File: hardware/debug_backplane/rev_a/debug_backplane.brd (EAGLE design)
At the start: 177.8 x 177.8 mm, 295 parts, among them IC3 FT232RQ, J0 BACKPLANE_GENERIC_MODULE_DEBUG, J1 BACKPLANE_GENERIC_MODULE_DEBUG, J2 PJ-102AH, J3 BACKPLANE_CONTROLLER_MODULE, J4 MICRO_USB_B_HIROSE_ZX62-B-5PA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, J5 MICRO_USB_B_HIROSE_ZX62-B-5PA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, J6 MICRO_USB_B_HIROSE_ZX62-B-5PA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, J8 MICRO_USB_B_HIROSE_ZX62-B-5PA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, J9 MICRO_USB_B_HIROSE_ZX62-B-5PA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, Q1 MOSFET-NCHANNELSMD, Q2 MOSFET-NCHANNELSMD, Q3 MOSFET-NCHANNELSMD, Q4 MOSFET-NCHANNELSMD, Q5 MOSFET-NCHANNELSMD, Q6 MOSFET-NCHANNELSMD, Q7 MOSFET-NCHANNELSMD, Q8 MOSFET-NCHANNELSMD, U1 TUSB2077A, U10 SAM4LC8AA, U11 LTC2941, U12 LTC2941, U13 FT232RQ, U14 SN74LVC2T45, U15 SN74LVC2T45, U16 FT232RQ, U2 FXMA2102, U20 TS3USB30E, U21 TS3USB30E, U26 MCP23008QFN, U27 MCP23008QFN, U3 FXMA2102, U4 MAX8887EZK33+T, U40 FT232RQ, U41 FT232RQ, U5 LTC2941, U6 PCA9544AQFN-N20, U7 LTC2941, U8 SN74LVC2T45, U9 SN74LVC2T45, X1 16MHz, Y1 ABMM

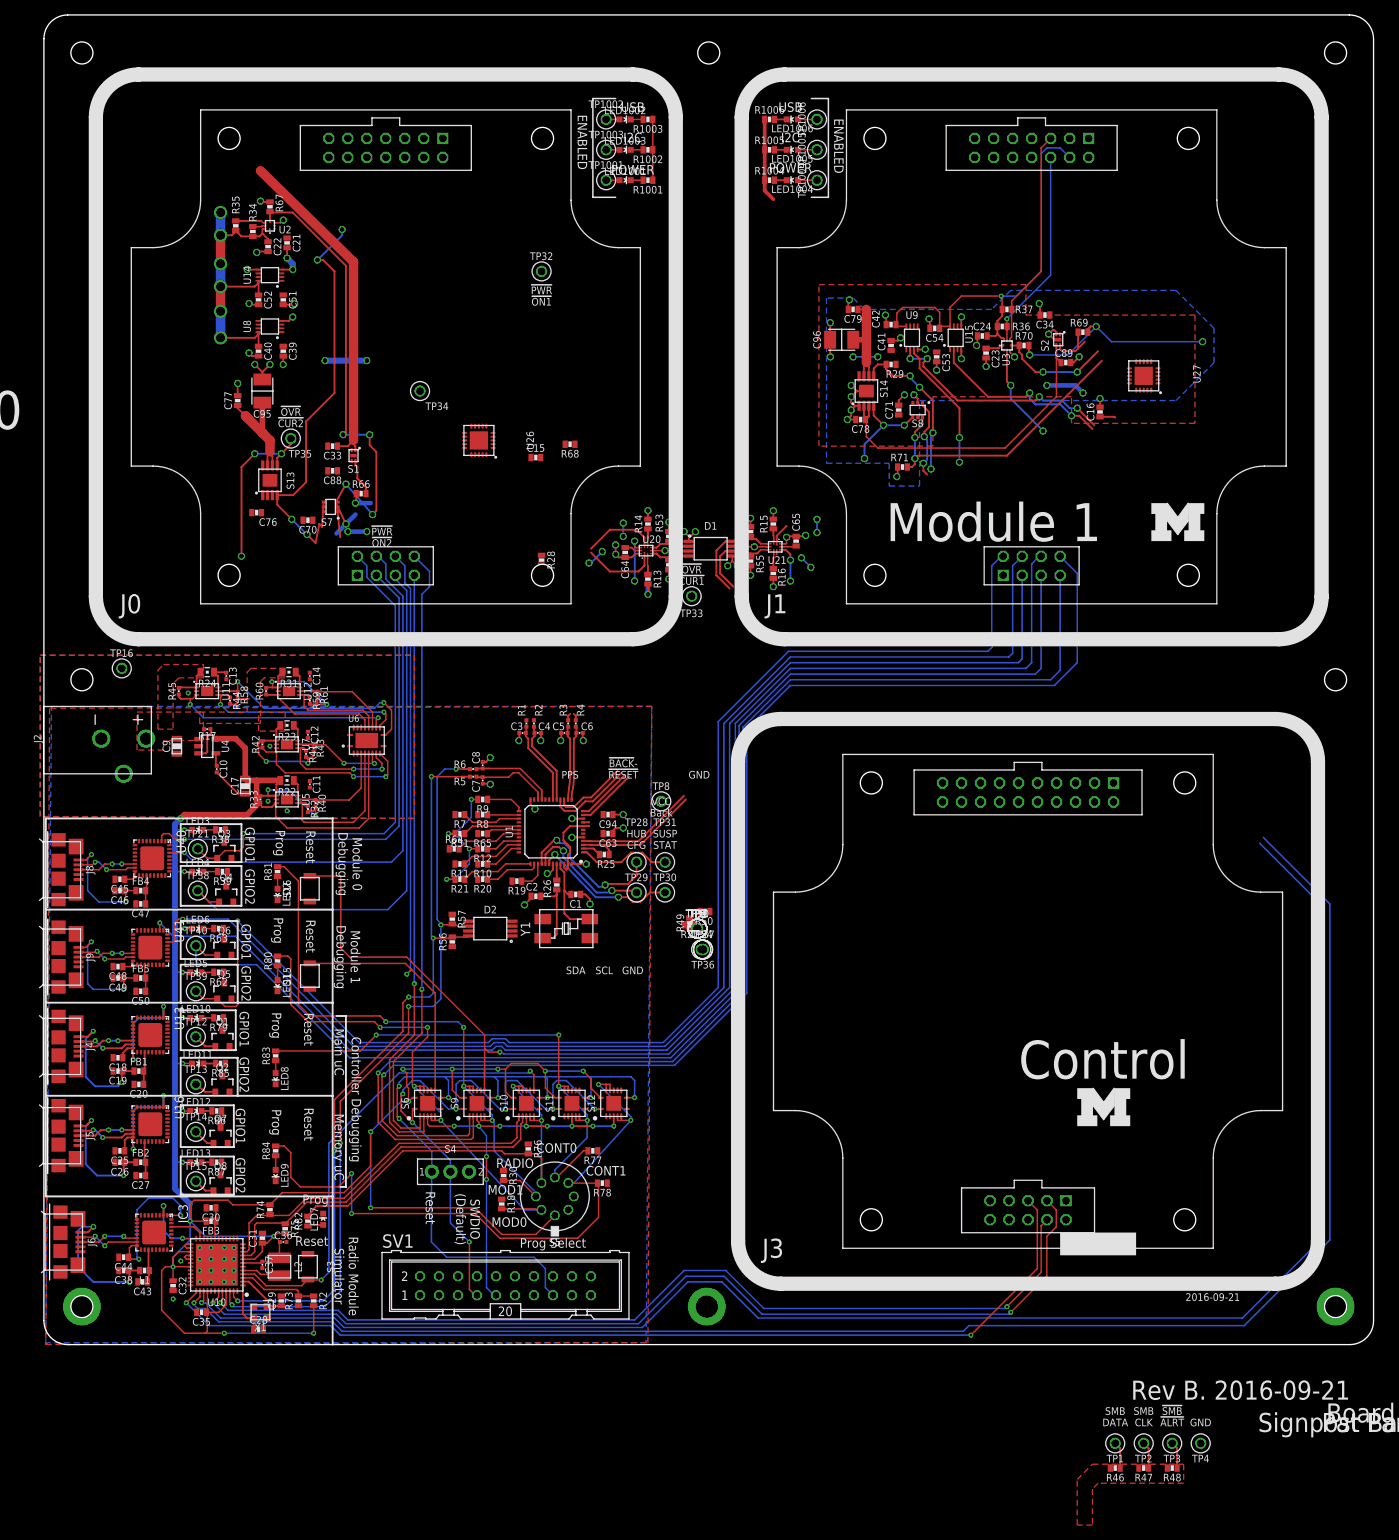
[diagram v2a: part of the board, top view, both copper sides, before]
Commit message: routing of controller debug signals
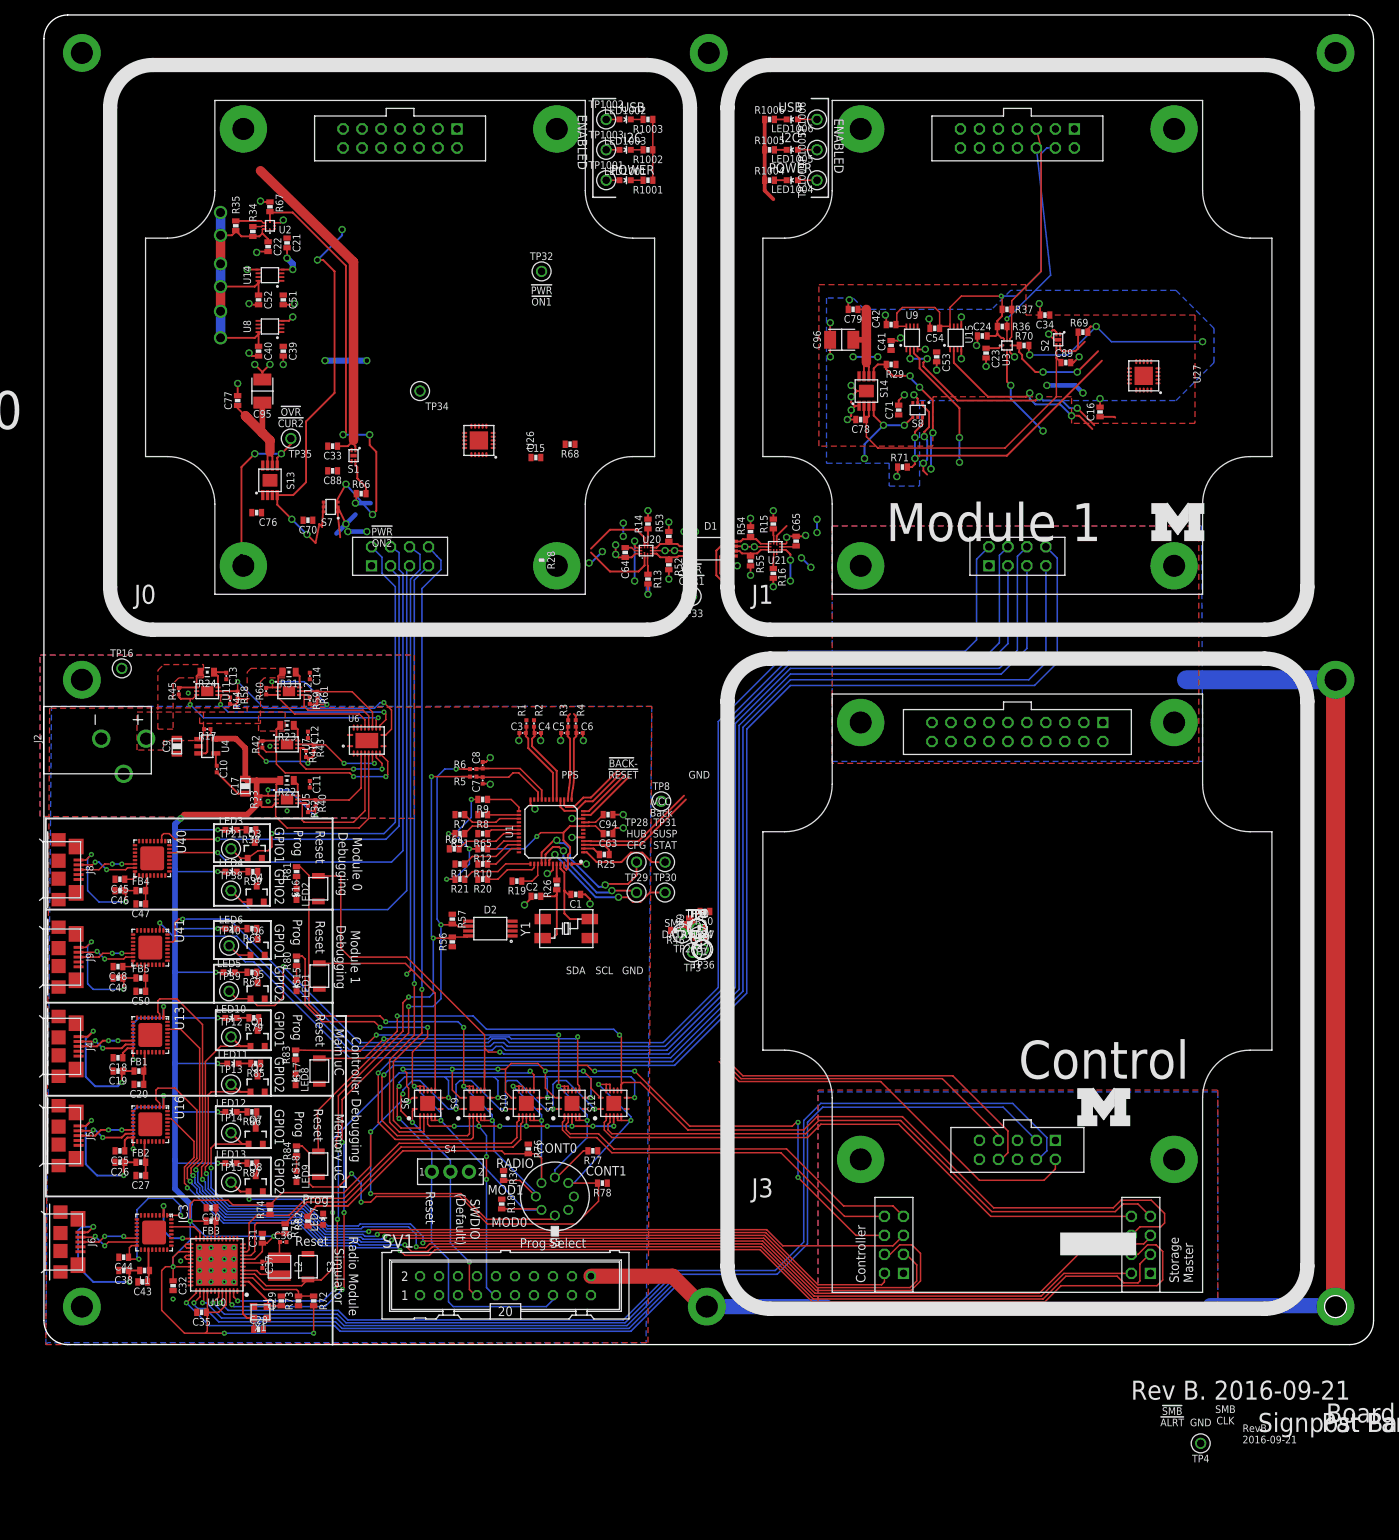
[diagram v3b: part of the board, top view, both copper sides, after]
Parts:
- added S17, S18: B3U-1000P, switches:B3U-1000P
- J3: value BACKPLANE_CONTROLLER_MODULE -> BACKPLANE_CONTROLLER_MODULE_DEBUG; device signpost:BACKPLANE_MODULE_20PIN_10PIN -> signpost:BACKPLANE_MODULE_20PIN_10PIN_DEBUG
- moved R48 96.0 mm to (87.6, 55.8)
- moved R46 92.9 mm to (84.5, 55.4)
- moved R47 92.5 mm to (87.8, 54.5)
- moved TP2 92.0 mm to (85.3, 55.0)
- moved TP3 91.8 mm to (86.7, 52.5)
- moved TP1 87.7 mm to (87.6, 54.6)
- moved J3 8.20 mm to (130.2, 54.0)
- moved Q7 4.70 mm to (28.3, 27.8)
- moved Q8 4.70 mm to (28.3, 21.5)
- moved LED12 4.70 mm to (25.0, 31.1)
- moved LED13 4.70 mm to (25.0, 24.3)
- moved R86 4.70 mm to (27.8, 31.1)
- moved R87 4.70 mm to (27.8, 24.3)
- moved TP14 4.70 mm to (25.0, 28.3)
- moved TP15 4.70 mm to (25.0, 21.7)
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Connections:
- removed net CONT00_DBG_GPIO2: Q2.1, TP13.TESTPOINT
- new net CONT0_DBG_GPIO2: J3.104, Q2.1, TP13.TESTPOINT
- net CONT0_!RESET: now also J3.105, S17.2
- net CONT0_DBG_GPIO1: now also J3.101
- net CONT0_DBG_RX: now also J3.103
- net CONT0_DBG_TX: now also J3.102
- net CONT0_SWDCLK: now also J3.106
- net CONT0_SWDIO: now also J3.107
- net CONT1_!RESET: now also J3.205, S18.2
- net CONT1_DBG_GPIO1: now also J3.201
- net CONT1_DBG_GPIO2: now also J3.204
- net CONT1_DBG_RX: now also J3.203
- net CONT1_DBG_TX: now also J3.202
- net CONT1_SWDCLK: now also J3.206
- net CONT1_SWDIO: now also J3.207
- net GND: now also J0.MNT1, J0.MNT2, J0.MNT3, J0.MNT4, J1.MNT1, J1.MNT2, J1.MNT3, J1.MNT4, J3.100, J3.200, J3.MNT1, J3.MNT2, J3.MNT3, J3.MNT4, S17.1, S18.1
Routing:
- net CONT1_DBG_TX: track 0.00 -> 159.8 mm, vias 0 -> 2
- net CONT1_DBG_RX: track 0.00 -> 159.3 mm, vias 0 -> 2
- net GND: track 150.7 -> 304.3 mm, vias 99 -> 104
- net CONT1_!RESET: track 0.00 -> 150.4 mm, vias 0 -> 2
- net CONT_MOD2_IN: track 218.4 -> 68.8 mm
- net CONT_MOD2_OUT: track 218.1 -> 71.2 mm
- net CONT1_DBG_GPIO1: track 2.98 -> 145.5 mm, vias 0 -> 2
- net CONT0_DBG_TX: track 0.00 -> 139.0 mm, vias 0 -> 2
- net CONT0_DBG_RX: track 0.00 -> 137.8 mm, vias 0 -> 2
- net CONT1_DBG_GPIO2: track 2.87 -> 134.0 mm, vias 0 -> 2
- net CONT0_DBG_GPIO1: track 3.13 -> 125.4 mm, vias 0 -> 2
- net CONT0_DBG_GPIO2: track 0.00 -> 118.6 mm, vias 0 -> 2
- net CONT0_!RESET: track 0.00 -> 98.4 mm, vias 0 -> 6
- net CONT1_SWDCLK: track 0.00 -> 81.6 mm
- net CONT1_SWDIO: track 0.00 -> 78.7 mm
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
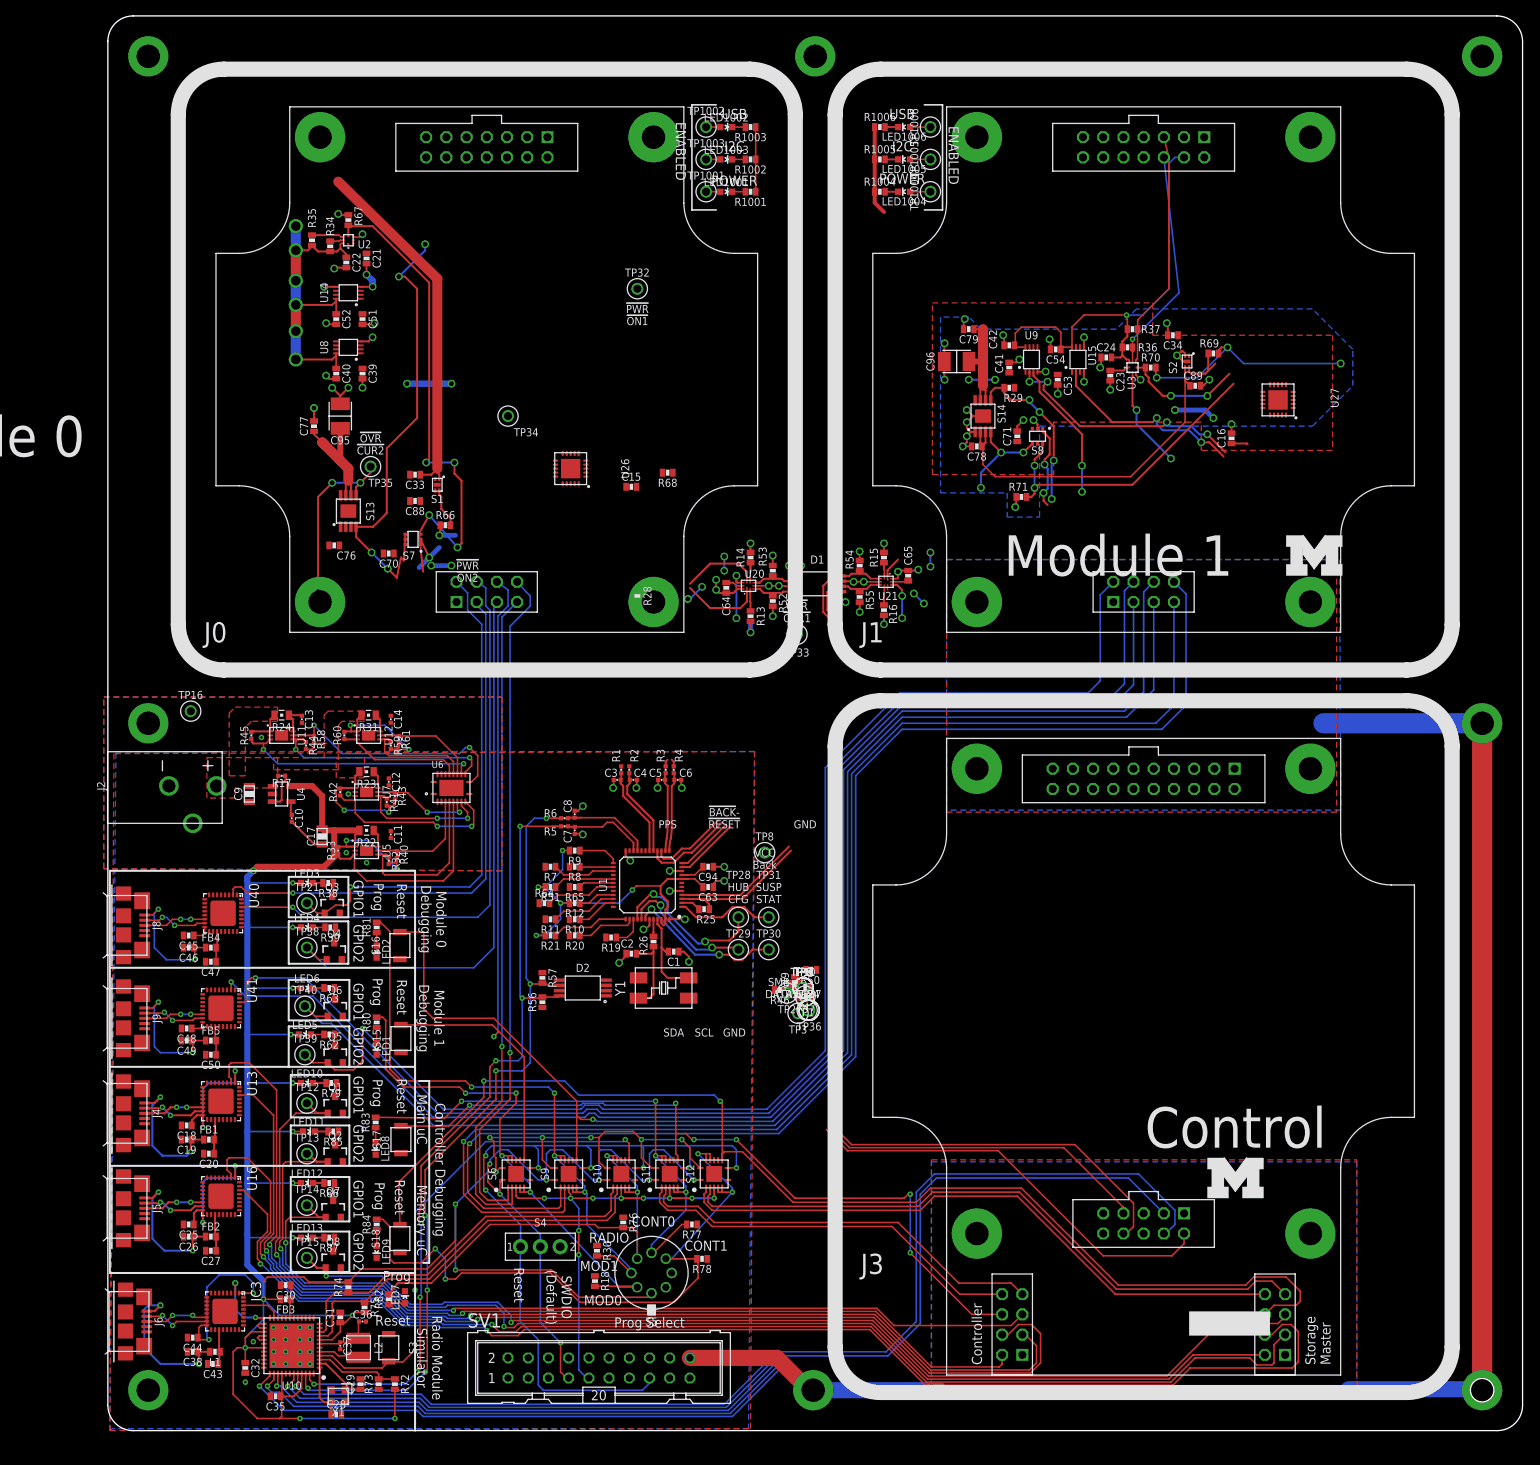
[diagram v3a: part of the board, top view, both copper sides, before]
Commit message: routed much of the isolation circuit
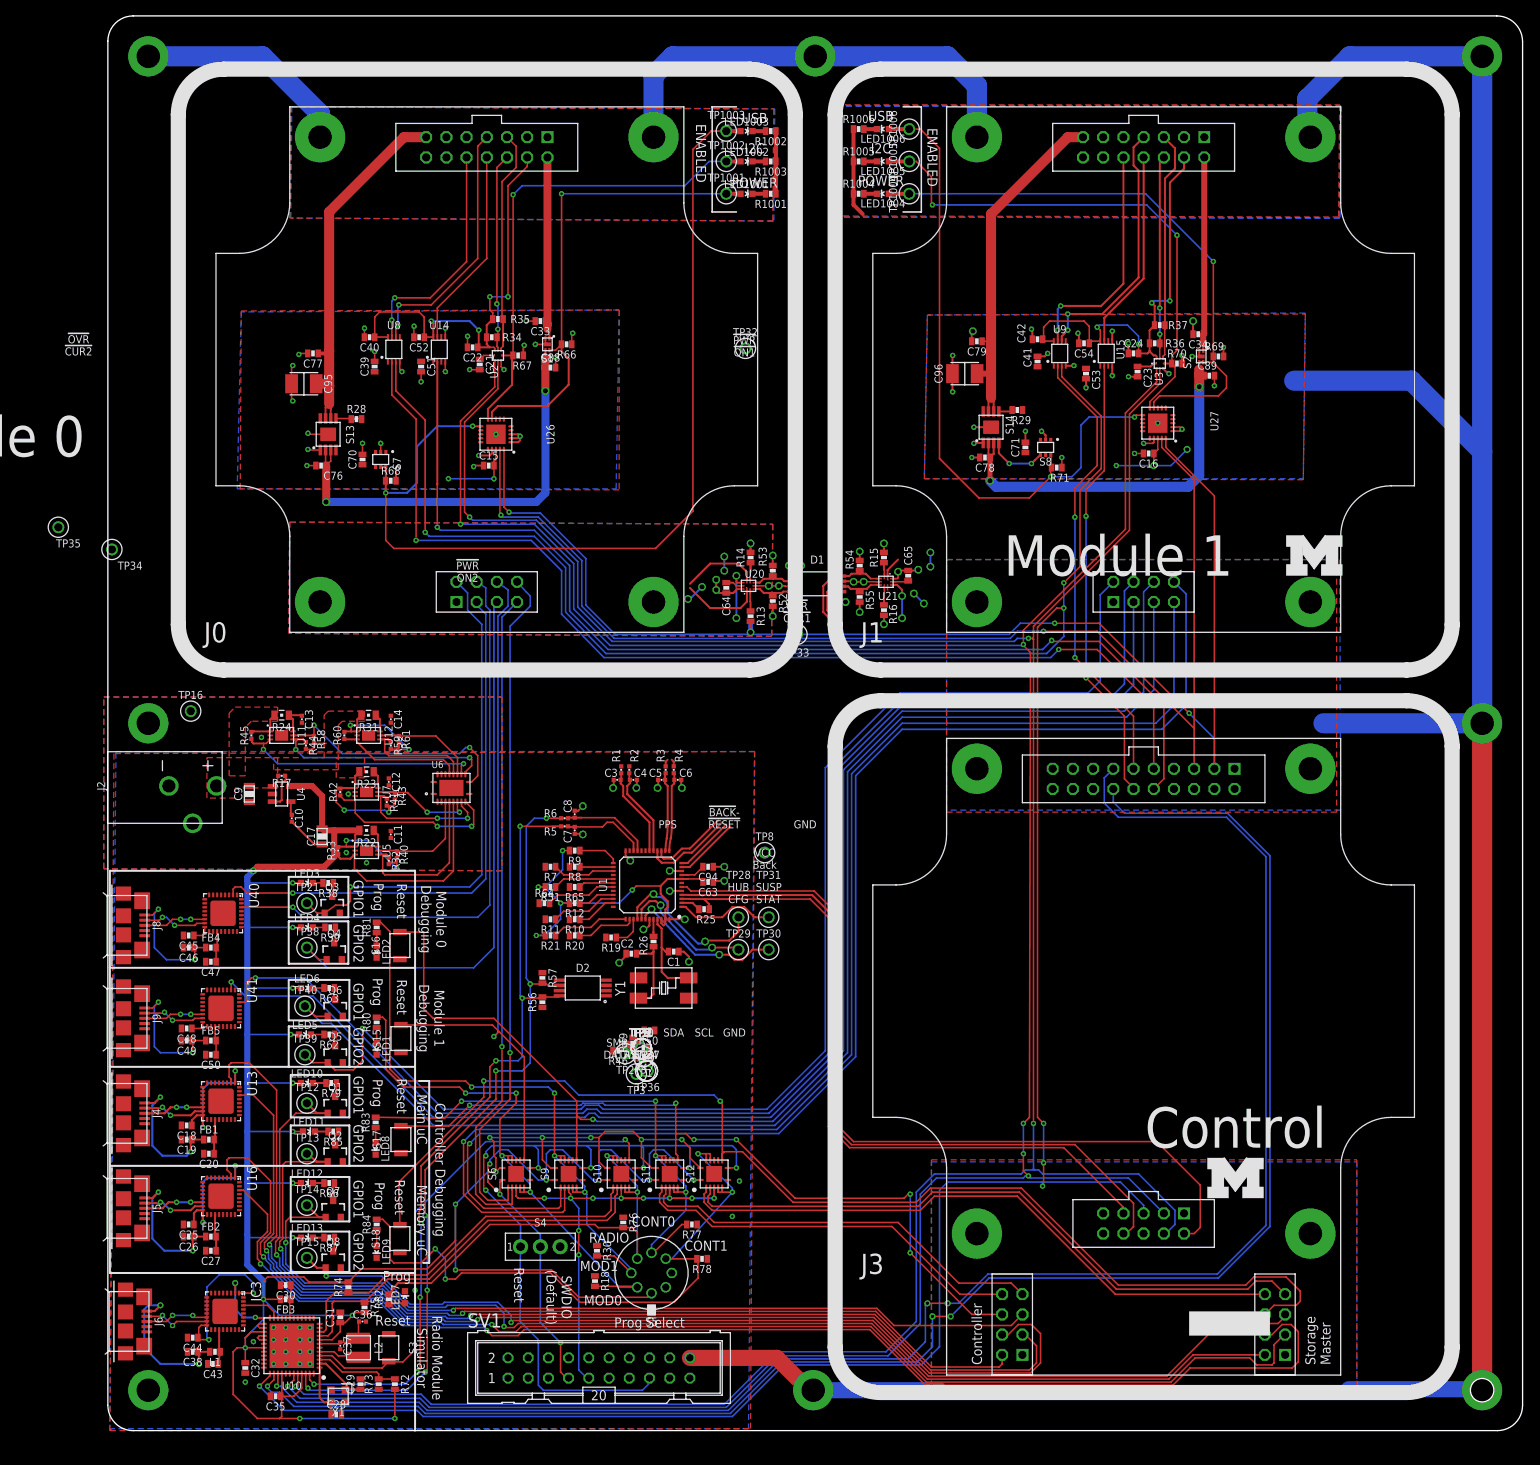
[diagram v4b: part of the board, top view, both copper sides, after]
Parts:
- moved TP34 52.5 mm to (0.51, 110.7)
- moved R28 41.7 mm to (31.2, 127.1), turned to 0 degrees
- moved TP35 40.0 mm to (-6.22, 113.5)
- moved R68 34.8 mm to (35.6, 119.4), turned to 180 degrees
- moved R66 27.4 mm to (57.7, 136.5), turned to 180 degrees
- moved R67 27.3 mm to (51.6, 135.1), turned to 180 degrees
- moved R35 25.4 mm to (49.0, 139.7), turned to 0 degrees
- moved C33 24.9 mm to (54.4, 139.4)
- moved C88 23.9 mm to (55.6, 133.6), turned to 0 degrees
- moved U2 23.7 mm to (49.0, 135.1), turned to 0 degrees
- moved R34 23.3 mm to (48.3, 137.4), turned to 0 degrees
- moved S1 22.4 mm to (55.2, 136.5)
- moved R47 21.7 mm to (67.4, 46.9)
- moved TP10 21.7 mm to (67.1, 48.0)
- moved TP11 21.7 mm to (67.1, 48.0)
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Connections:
- removed net N$33: R69.1, R70.1, R71.1, U27.17, U27.GND
- net GND: now also R69.1, R70.1, R71.1, U27.17, U27.GND
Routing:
- net PPS: track 90.2 -> 368.0 mm, vias 3 -> 7
- net GND: track 304.3 -> 542.5 mm, vias 104 -> 123
- net MOD_SDA: track 136.4 -> 348.9 mm, vias 1 -> 6
- net MOD_SCL: track 153.4 -> 350.5 mm, vias 3 -> 4
- net SMBDATA: track 0.00 -> 161.0 mm, vias 0 -> 3
- net SMBCLK: track 0.00 -> 153.8 mm, vias 0 -> 2
- net CONT_MOD2_IN: track 68.8 -> 213.8 mm, vias 1 -> 3
- net CONT_MOD2_OUT: track 71.2 -> 212.2 mm, vias 1 -> 3
- net CONT_MOD0_IN: track 0.00 -> 137.0 mm, vias 0 -> 2
- net CONT_MOD0_OUT: track 0.00 -> 136.7 mm, vias 0 -> 2
- net MOD0_ISO_USB: track 1.79 -> 120.7 mm, vias 0 -> 2
- net MOD1_ISO_POWER: track 9.21 -> 72.8 mm, vias 0 -> 1
- net MOD0_USB_!EN: track 64.4 -> 6.76 mm, vias 6 -> 2
- net MOD0_5V_METERED: track 3.93 -> 58.7 mm, vias 0 -> 2
- net MOD0_ISO_POWER: track 6.73 -> 60.7 mm, vias 0 -> 1
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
